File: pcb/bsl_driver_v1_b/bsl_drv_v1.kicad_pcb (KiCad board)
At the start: 4 copper layers, 86 x 34 mm, 159 parts, among them J101 2005WR-2x10P, J102 PJ-320D-4A, J201 TYPE-C-31-M-12, J202 TYPE-C-31-M-12, Q101 BSS138, SW101 TS-1187A, SW102 TS-1187A, SW103 TS-1187A, U1001 TPS61169, U101 W25Q16JVSNIQ, U102 RP2040, U1101 TPS61169, U201 CH221K, U202 HT7533-1, U301 TPS61169, U401 TPS61169, U501 TPS61169, U601 TPS61169, U701 TPS61169, U801 TPS61169, U901 TPS61169, Y101 ABM8-272-T3

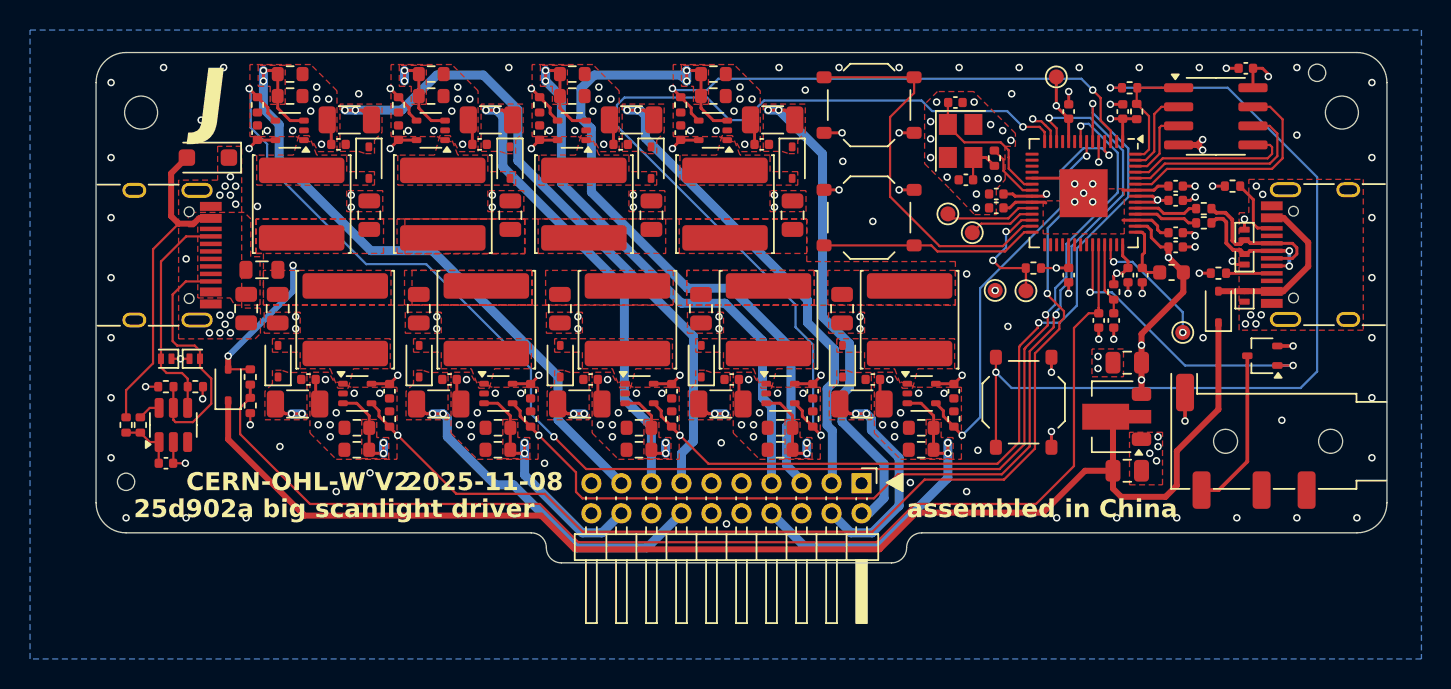
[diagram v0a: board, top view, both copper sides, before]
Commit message: remove csv from gitignore, regenerate BOMs and schematics
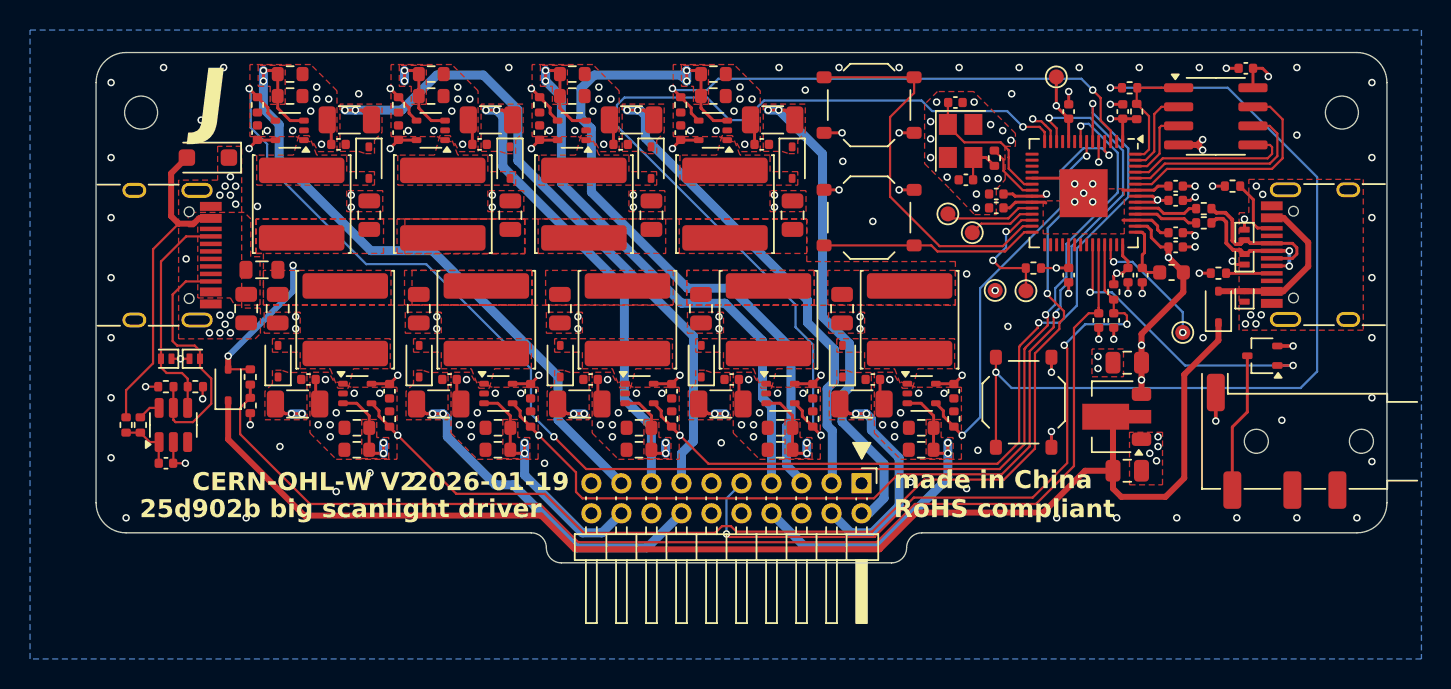
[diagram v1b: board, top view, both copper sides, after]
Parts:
- removed H103, H104: tooling hole, MountingHole:ToolingHole_1.152mm
- moved J102 2.05 mm to (119.5, 111.4)
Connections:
- C116 pad 1: /TH+ -> /TH
- R109 pad 2: /TH+ -> /TH
- U102 pad 39: /TH+ -> /TH
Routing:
- net /TH: track 0.00 -> 47.6 mm, vias 0 -> 3
- net /TH+: track 4.81 -> 0.00 mm
- net Net-(Q101-D): track 10.9 -> 9.36 mm
- net GND: vias 212 -> 211
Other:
- board text added: "2026-01-19"
- board text added: "25d902b big scanlight driver"
- board text added: "made in China RoHS compliant"
- board text removed: "2025-11-08"
- board text removed: "25d902a big scanlight driver"
- board text removed: "assembled in China"
